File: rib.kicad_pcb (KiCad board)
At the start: 2 copper layers, 140 x 90 mm, 89 parts, among them J1 RJ45_LED, J10 Conn_01x04_Male, J11 Screw_Terminal_01x02, J12 Screw_Terminal_01x02, J13 Screw_Terminal_01x02, J14 Conn_01x02_Male, J15 Conn_01x02_Male, J16 Conn_01x06_Male, J2 RJ45_LED, J3 RJ45_LED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

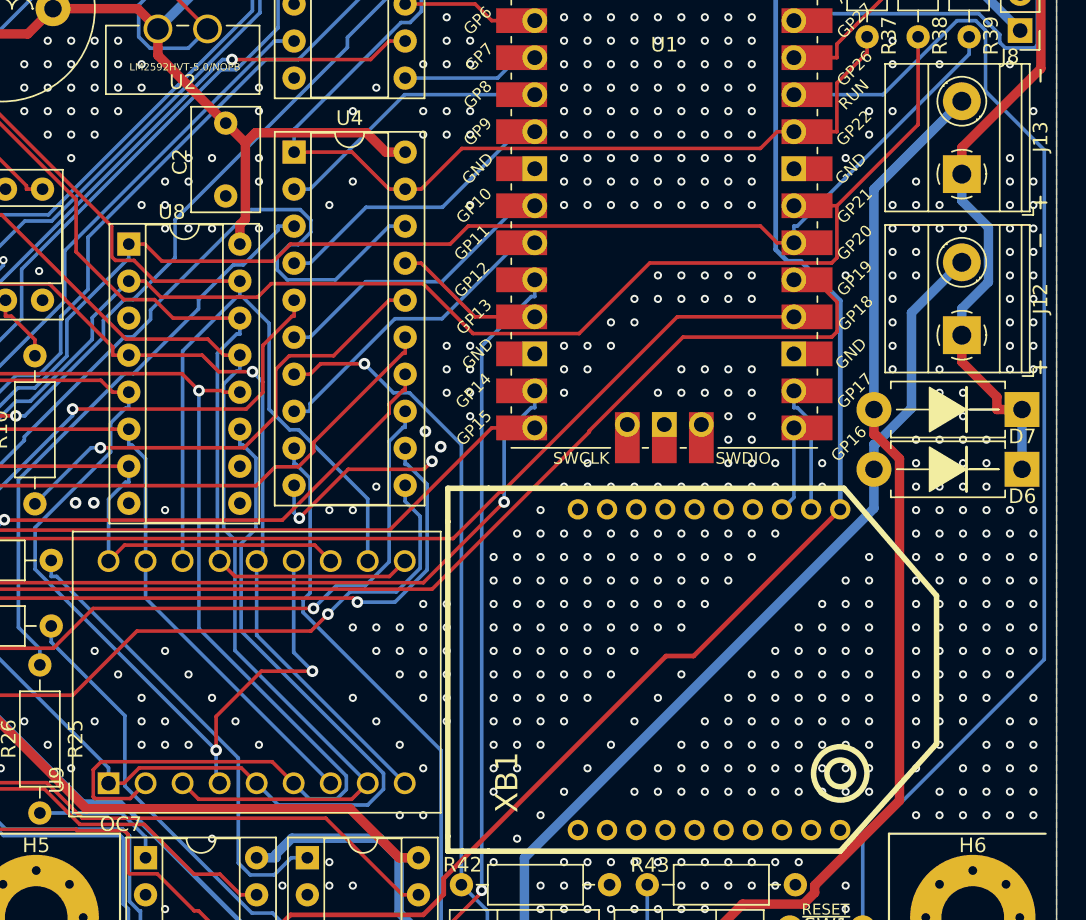
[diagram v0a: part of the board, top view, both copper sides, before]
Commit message: Add RGB LEDs
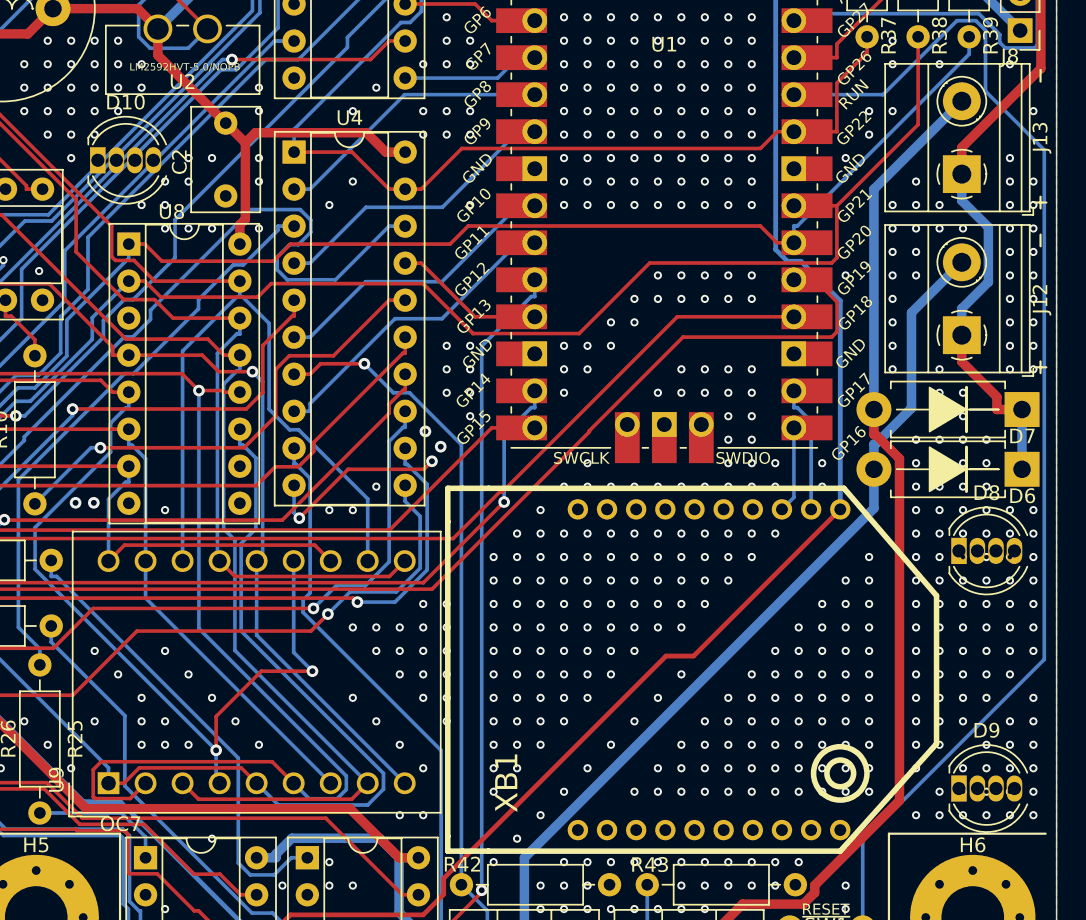
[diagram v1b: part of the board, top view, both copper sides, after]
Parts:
- added D10: LED_RKBG, LED_THT:LED_D5.0mm-4_RGB, F.Cu at (109.7, 79.3)
- added D8: LED_RKBG, LED_THT:LED_D5.0mm-4_RGB, F.Cu at (168.8, 106.1)
- added D9: LED_RKBG, LED_THT:LED_D5.0mm-4_RGB, F.Cu at (168.8, 122.4)
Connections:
- U8 pad 3: unconnected-(U8-Pad3) -> Net-(U8-Pad3)
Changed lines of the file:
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@@
   (net 148 "SDA")
   (net 149 "SCL")
-  (net 150 "unconnected-(U8-Pad3)")
+  (net 150 "Net-(U8-Pad3)")
   (net 151 "unconnected-(U8-Pad9)")
   (net 152 "unconnected-(U8-Pad10)")
@@
     )
   )
+  (footprint "LED_THT:LED_D5.0mm-4_RGB" (layer "F.Cu")
+    (at 168.8 122.4)
+    (descr "LED, diameter 5.0mm, 4 pins, WP154A4, https://www.kingbright.com/attachments/file/psearch/000/00/00/L-154A4SUREQBFZGEW(Ver.11A).pdf")
+    (tags "LED diameter 5.0mm 2 pins diameter 5.0mm 3 pins diameter 5.0mm 4 pins RGB RGBLED")
+    (property "Sheetfile" "rib.kicad_sch")
+    (property "Sheetname" "")
+    (attr through_hole)
+    (fp_text reference "D9" (at 1.905 -3.96) (layer "F.SilkS")
+      (effects (font (size 1 1) (thickness 0.15)))
+    )
+    (fp_text value "LED_RKBG" (at 1.905 3.96) (layer "F.Fab")
+      (effects (font (size 1 1) (thickness 0.15)))
+    )
+    (fp_text user "${REFERENCE}" (at 1.905 -3.96) (layer "F.Fab")
+      (effects (font (size 1 1) (thickness 0.15)))
+    )
+    (fp_line (start -0.655 1.08) (end -0.655 1.545) (layer "F.SilkS") (width 0.12))
+    (fp_line (start -0.655 -1.545) (end -0.655 -1.08) (layer "F.SilkS") (width 0.12))
+    (fp_arc (start -0.655 -1.54483) (mid 2.163456 -2.978809) (end 4.692815 -1.080827) (layer "F.SilkS") (width 0.12))
+    (fp_arc (start 4.159479 1.080429) (mid 1.904762 2.5) (end -0.349684 1.08) (layer "F.SilkS") (width 0.12))
+    (fp_arc (start -0.349684 -1.08) (mid 1.904762 -2.5) (end 4.159479 -1.080429) (layer "F.SilkS") (width 0.12))
+    (fp_arc (start 4.692815 1.080827) (mid 2.163456 2.978808) (end -0.655 1.54483) (layer "F.SilkS") (width 0.12))
+    (fp_line (start 5.15 3.25) (end 5.15 -3.25) (layer "F.CrtYd") (width 0.05))
+    (fp_line (start -1.35 3.25) (end 5.15 3.25) (layer "F.CrtYd") (width 0.05))
+    (fp_line (start 5.15 -3.25) (end -1.35 -3.25) (layer "F.CrtYd") (width 0.05))
+    (fp_line (start -1.35 -3.25) (end -1.35 3.25) (layer "F.CrtYd") (width 0.05))
+    (fp_line (start -0.595 -1.469694) (end -0.595 1.469694) (layer "F.Fab") (width 0.1))
+    (fp_arc (start -0.595 -1.469694) (mid 4.805 0.000016) (end -0.595016 1.469666) (layer "F.Fab") (width 0.1))
+    (fp_circle (center 1.905 0) (end 4.405 0) (layer "F.Fab") (width 0.1) (fill none))
+    (pad "1" thru_hole rect (at 0 0) (size 1.07 1.8) (drill 0.9) (layers *.Cu *.Mask)
+      (net 137 "LED5") (pinfunction "RA") (pintype "passive"))
+    (pad "2" thru_hole oval (at 1.27 0) (size 1.07 1.8) (drill 0.9) (layers *.Cu *.Mask)
+      (net 133 "LED1") (pinfunction "K") (pintype "passive"))
+    (pad "3" thru_hole oval (at 2.54 0) (size 1.07 1.8) (drill 0.9) (layers *.Cu *.Mask)
+      (net 139 "LED7") (pinfunction "BA") (pintype "passive"))
+    (pad "4" thru_hole oval (at 3.81 0) (size 1.07 1.8) (drill 0.9) (layers *.Cu *.Mask)
+      (net 136 "LED6") (pinfunction "GA") (pintype "passive"))
+    (model "${KICAD6_3DMODEL_DIR}/LED_THT.3dshapes/LED_D5.0mm-4_RGB.wrl"
+      (offset (xyz 0 0 0))
+      (scale (xyz 1 1 1))
+      (rotate (xyz 0 0 0))
+    )
+  )
   (footprint "MountingHole:MountingHole_4.3mm_M4_Pad_Via" (layer "F.Cu")
     (at 169.75 131.25)
@@
       (net 149 "SCL") (pinfunction "SCL") (pintype "input"))
     (pad "3" thru_hole oval (at 0 5.08) (size 1.6 1.6) (drill 0.8) (layers *.Cu *.Mask)
-      (net 150 "unconnected-(U8-Pad3)") (pinfunction "IRQ/SEG9") (pintype "output"))
+      (net 150 "Net-(U8-Pad3)") (pinfunction "IRQ/SEG9") (pintype "output"))
     (pad "4" thru_hole oval (at 0 7.62) (size 1.6 1.6) (drill 0.8) (layers *.Cu *.Mask)
       (net 138 "LED8") (pinfunction "DIG0/SEG0") (pintype "output"))
@@
     )
   )
+  (footprint "LED_THT:LED_D5.0mm-4_RGB" (layer "F.Cu")
+    (at 168.8 106.1)
+    (descr "LED, diameter 5.0mm, 4 pins, WP154A4, https://www.kingbright.com/attachments/file/psearch/000/00/00/L-154A4SUREQBFZGEW(Ver.11A).pdf")
+    (tags "LED diameter 5.0mm 2 pins diameter 5.0mm 3 pins diameter 5.0mm 4 pins RGB RGBLED")
+    (property "Sheetfile" "rib.kicad_sch")
+    (property "Sheetname" "")
+    (attr through_hole)
+    (fp_text reference "D8" (at 1.905 -3.96) (layer "F.SilkS")
+      (effects (font (size 1 1) (thickness 0.15)))
+    )
+    (fp_text value "LED_RKBG" (at 1.905 3.96) (layer "F.Fab")
+      (effects (font (size 1 1) (thickness 0.15)))
+    )
+    (fp_text user "${REFERENCE}" (at 1.905 -3.96) (layer "F.Fab")
+      (effects (font (size 1 1) (thickness 0.15)))
+    )
+    (fp_line (start -0.655 1.08) (end -0.655 1.545) (layer "F.SilkS") (width 0.12))
+    (fp_line (start -0.655 -1.545) (end -0.655 -1.08) (layer "F.SilkS") (width 0.12))
+    (fp_arc (start -0.349684 -1.08) (mid 1.904762 -2.5) (end 4.159479 -1.080429) (layer "F.SilkS") (width 0.12))
+    (fp_arc (start -0.655 -1.54483) (mid 2.163456 -2.978809) (end 4.692815 -1.080827) (layer "F.SilkS") (width 0.12))
+    (fp_arc (start 4.692815 1.080827) (mid 2.163456 2.978808) (end -0.655 1.54483) (layer "F.SilkS") (width 0.12))
+    (fp_arc (start 4.159479 1.080429) (mid 1.904762 2.5) (end -0.349684 1.08) (layer "F.SilkS") (width 0.12))
+    (fp_line (start -1.35 3.25) (end 5.15 3.25) (layer "F.CrtYd") (width 0.05))
+    (fp_line (start 5.15 3.25) (end 5.15 -3.25) (layer "F.CrtYd") (width 0.05))
+    (fp_line (start -1.35 -3.25) (end -1.35 3.25) (layer "F.CrtYd") (width 0.05))
+    (fp_line (start 5.15 -3.25) (end -1.35 -3.25) (layer "F.CrtYd") (width 0.05))
+    (fp_line (start -0.595 -1.469694) (end -0.595 1.469694) (layer "F.Fab") (width 0.1))
+    (fp_arc (start -0.595 -1.469694) (mid 4.805 0.000016) (end -0.595016 1.469666) (layer "F.Fab") (width 0.1))
+    (fp_circle (center 1.905 0) (end 4.405 0) (layer "F.Fab") (width 0.1) (fill none))
+    (pad "1" thru_hole rect (at 0 0) (size 1.07 1.8) (drill 0.9) (layers *.Cu *.Mask)
+      (net 132 "LED2") (pinfunction "RA") (pintype "passive"))
+    (pad "2" thru_hole oval (at 1.27 0) (size 1.07 1.8) (drill 0.9) (layers *.Cu *.Mask)
+      (net 133 "LED1") (pinfunction "K") (pintype "passive"))
+    (pad "3" thru_hole oval (at 2.54 0) (size 1.07 1.8) (drill 0.9) (layers *.Cu *.Mask)
+      (net 134 "LED4") (pinfunction "BA") (pintype "passive"))
+    (pad "4" thru_hole oval (at 3.81 0) (size 1.07 1.8) (drill 0.9) (layers *.Cu *.Mask)
+      (net 135 "LED3") (pinfunction "GA") (pintype "passive"))
+    (model "${KICAD6_3DMODEL_DIR}/LED_THT.3dshapes/LED_D5.0mm-4_RGB.wrl"
+      (offset (xyz 0 0 0))
+      (scale (xyz 1 1 1))
+      (rotate (xyz 0 0 0))
+    )
+  )
   (footprint "Resistor_THT:R_Array_SIP6" (layer "F.Cu")
     (at 63.1 77.25)
@@
       (offset (xyz 0 0 0))
       (scale (xyz 1 1 1))
+      (rotate (xyz 0 0 0))
+    )
+  )
+  (footprint "LED_THT:LED_D5.0mm-4_RGB" (layer "F.Cu")
+    (at 109.73 79.3)
+    (descr "LED, diameter 5.0mm, 4 pins, WP154A4, https://www.kingbright.com/attachments/file/psearch/000/00/00/L-154A4SUREQBFZGEW(Ver.11A).pdf")
+    (tags "LED diameter 5.0mm 2 pins diameter 5.0mm 3 pins diameter 5.0mm 4 pins RGB RGBLED")
+    (property "Sheetfile" "rib.kicad_sch")
+    (property "Sheetname" "")
+    (attr through_hole)
+    (fp_text reference "D10" (at 1.905 -3.96) (layer "F.SilkS")
+      (effects (font (size 1 1) (thickness 0.15)))
+    )
+    (fp_text value "LED_RKBG" (at 1.905 3.96) (layer "F.Fab")
+      (effects (font (size 1 1) (thickness 0.15)))
+    )
+    (fp_text user "${REFERENCE}" (at 1.905 -3.96) (layer "F.Fab")
+      (effects (font (size 1 1) (thickness 0.15)))
+    )
+    (fp_line (start -0.655 -1.545) (end -0.655 -1.08) (layer "F.SilkS") (width 0.12))
+    (fp_line (start -0.655 1.08) (end -0.655 1.545) (layer "F.SilkS") (width 0.12))
+    (fp_arc (start -0.349684 -1.08) (mid 1.904762 -2.5) (end 4.159479 -1.080429) (layer "F.SilkS") (width 0.12))
+    (fp_arc (start 4.692815 1.080827) (mid 2.163456 2.978808) (end -0.655 1.54483) (layer "F.SilkS") (width 0.12))
+    (fp_arc (start 4.159479 1.080429) (mid 1.904762 2.5) (end -0.349684 1.08) (layer "F.SilkS") (width 0.12))
+    (fp_arc (start -0.655 -1.54483) (mid 2.163456 -2.978809) (end 4.692815 -1.080827) (layer "F.SilkS") (width 0.12))
+    (fp_line (start -1.35 -3.25) (end -1.35 3.25) (layer "F.CrtYd") (width 0.05))
+    (fp_line (start -1.35 3.25) (end 5.15 3.25) (layer "F.CrtYd") (width 0.05))
+    (fp_line (start 5.15 -3.25) (end -1.35 -3.25) (layer "F.CrtYd") (width 0.05))
+    (fp_line (start 5.15 3.25) (end 5.15 -3.25) (layer "F.CrtYd") (width 0.05))
+    (fp_line (start -0.595 -1.469694) (end -0.595 1.469694) (layer "F.Fab") (width 0.1))
+    (fp_arc (start -0.595 -1.469694) (mid 4.805 0.000016) (end -0.595016 1.469666) (layer "F.Fab") (width 0.1))
+    (fp_circle (center 1.905 0) (end 4.405 0) (layer "F.Fab") (width 0.1) (fill none))
+    (pad "1" thru_hole rect (at 0 0) (size 1.07 1.8) (drill 0.9) (layers *.Cu *.Mask)
+      (net 138 "LED8") (pinfunction "RA") (pintype "passive"))
+    (pad "2" thru_hole oval (at 1.27 0) (size 1.07 1.8) (drill 0.9) (layers *.Cu *.Mask)
+      (net 133 "LED1") (pinfunction "K") (pintype "passive"))
+    (pad "3" thru_hole oval (at 2.54 0) (size 1.07 1.8) (drill 0.9) (layers *.Cu *.Mask)
+      (net 150 "Net-(U8-Pad3)") (pinfunction "BA") (pintype "passive"))
+    (pad "4" thru_hole oval (at 3.81 0) (size 1.07 1.8) (drill 0.9) (layers *.Cu *.Mask)
+      (net 147 "CATHODE3") (pinfunction "GA") (pintype "passive"))
+    (model "${KICAD6_3DMODEL_DIR}/LED_THT.3dshapes/LED_D5.0mm-4_RGB.wrl"
+      (offset (xyz 0 0 0))
+      (scale (xyz 1 1 1))

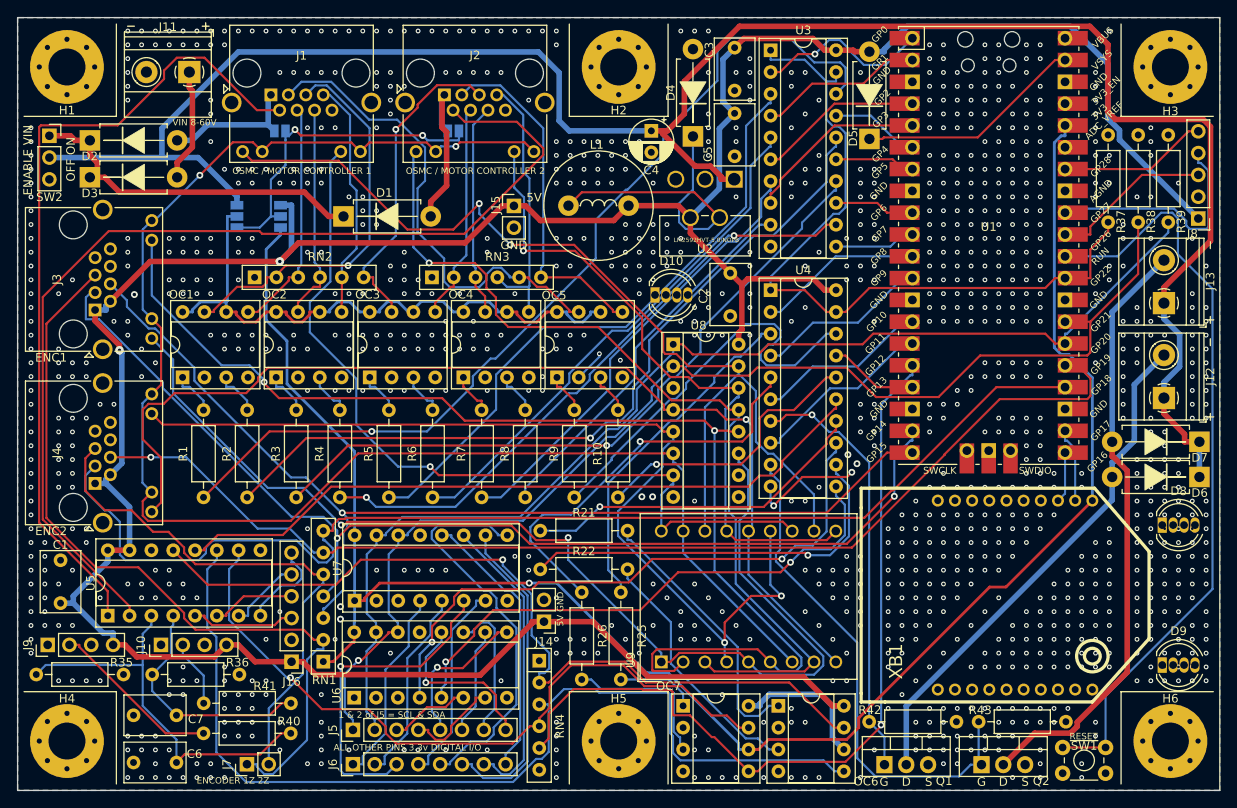
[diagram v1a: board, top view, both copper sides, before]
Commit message: Add RGB LEDs
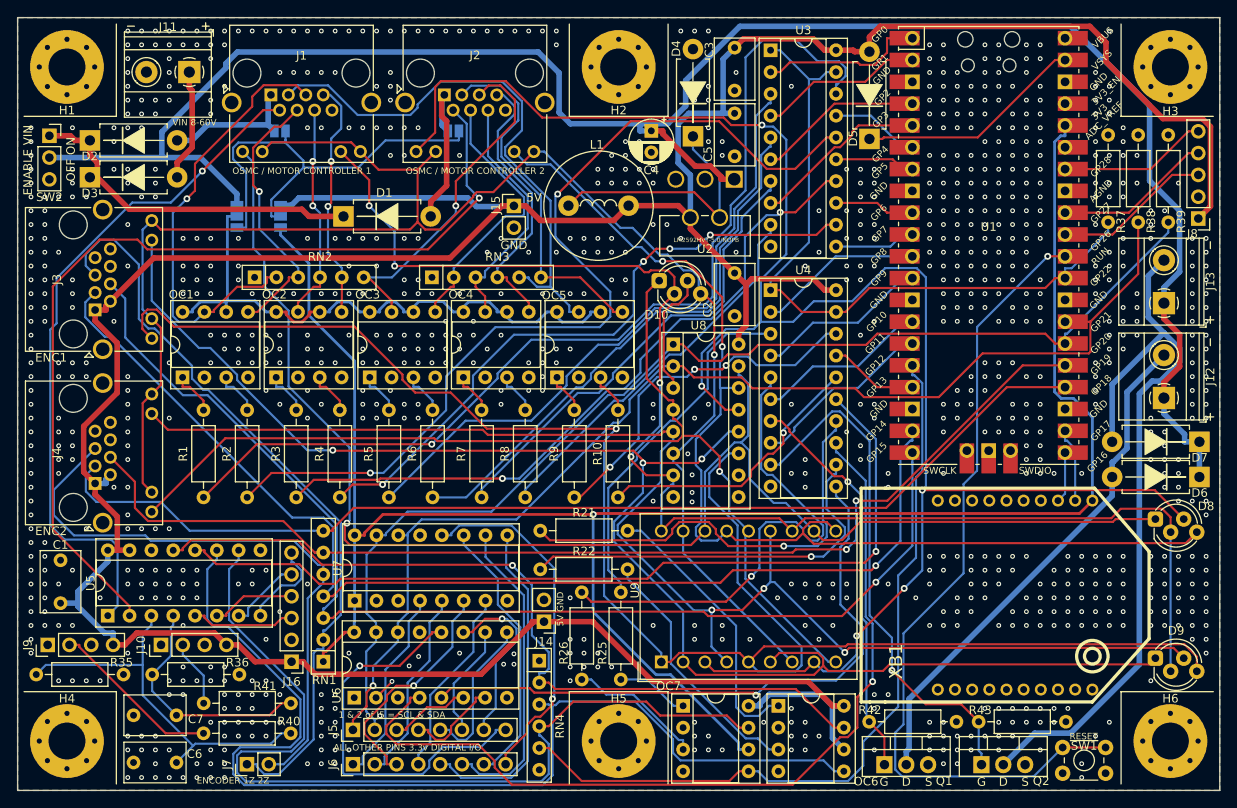
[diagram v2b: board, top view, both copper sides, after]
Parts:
- D10, D8, D9: footprint LED_THT:LED_D5.0mm-4_RGB -> LED_THT:LED_D5.0mm-4_RGB_Staggered_Pins
- moved D10 1.73 mm to (110.2, 77.6)
- moved D9 1.13 mm to (168.0, 121.6)
- moved D8 1.06 mm to (168.0, 105.4)
- moved C2 0.50 mm to (119.0, 81.8)
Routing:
- net LED4: track 106.7 -> 213.8 mm, vias 1 -> 5
- net LED6: track 130.5 -> 199.7 mm, vias 2 -> 1
- net LED1: track 98.3 -> 165.5 mm, vias 1 -> 4
- net LED2: track 115.7 -> 171.7 mm, vias 2 -> 1
- net LED3: track 76.9 -> 128.9 mm, vias 1 -> 2
- net LED7: track 114.8 -> 164.4 mm, vias 2 -> 3
- net LED5: track 138.0 -> 177.8 mm, vias 2 -> 3
- net Net-(U4-Pad13): track 70.8 -> 102.7 mm, vias 2 -> 1
- net 5V: track 371.6 -> 403.1 mm, vias 2 -> 0
- net Net-(J5-Pad8): track 19.9 -> 46.3 mm
- net Net-(OC7-Pad7): track 84.2 -> 106.6 mm, vias 1 -> 0
- net Net-(U4-Pad15): track 83.1 -> 102.3 mm, vias 0 -> 1
- net Net-(R2-Pad1): track 92.0 -> 110.1 mm, vias 1 -> 2
- net Net-(D7-Pad2): track 70.5 -> 87.7 mm
- net 3.3V: track 212.7 -> 227.9 mm
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
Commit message: Fix keepouts for screwholes, update parts list
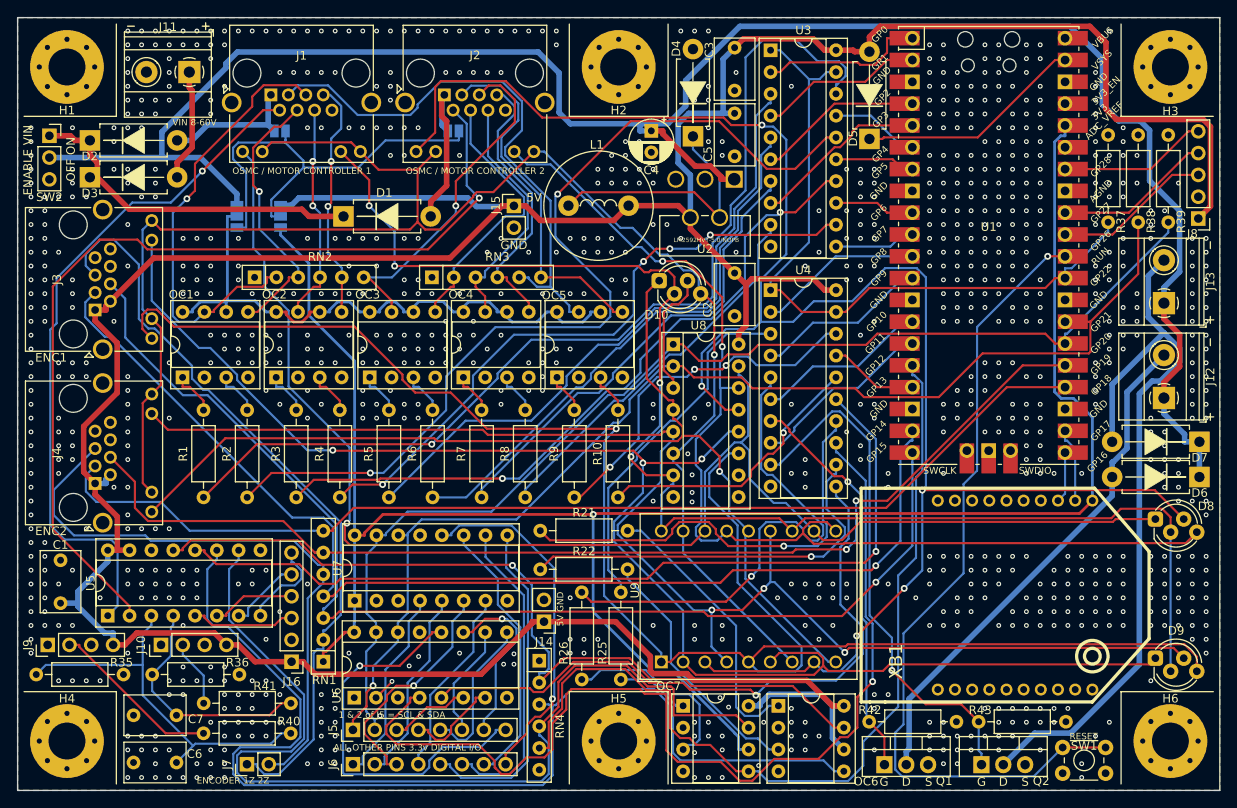
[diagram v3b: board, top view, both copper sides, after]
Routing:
- net Net-(U4-Pad13): track 102.7 -> 117.2 mm
- net Net-(OC7-Pad5): track 91.1 -> 103.8 mm
- net Net-(OC7-Pad7): track 106.6 -> 113.6 mm
- net Net-(OC7-Pad3): track 15.8 -> 22.3 mm
- net 5V: track 403.1 -> 407.4 mm
- net Net-(OC6-Pad5): track 125.0 -> 128.3 mm
- net Net-(U4-Pad11): track 73.4 -> 76.3 mm
- net Net-(OC6-Pad7): track 95.2 -> 97.5 mm
- net VIN: track 227.7 -> 229.2 mm
- net GND: vias 1000 -> 1004
